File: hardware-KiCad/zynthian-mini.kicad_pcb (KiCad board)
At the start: 2 copper layers, 163 x 120 mm, 76 parts, among them SW1 SW_Push, SW10 SW_Push, SW11 SW_Push, SW12 SW_Push, SW13 SW_Push, SW14 SW_Push, SW15 SW_Push, SW16 SW_Push, SW17 SW_Push, SW18 SW_Push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

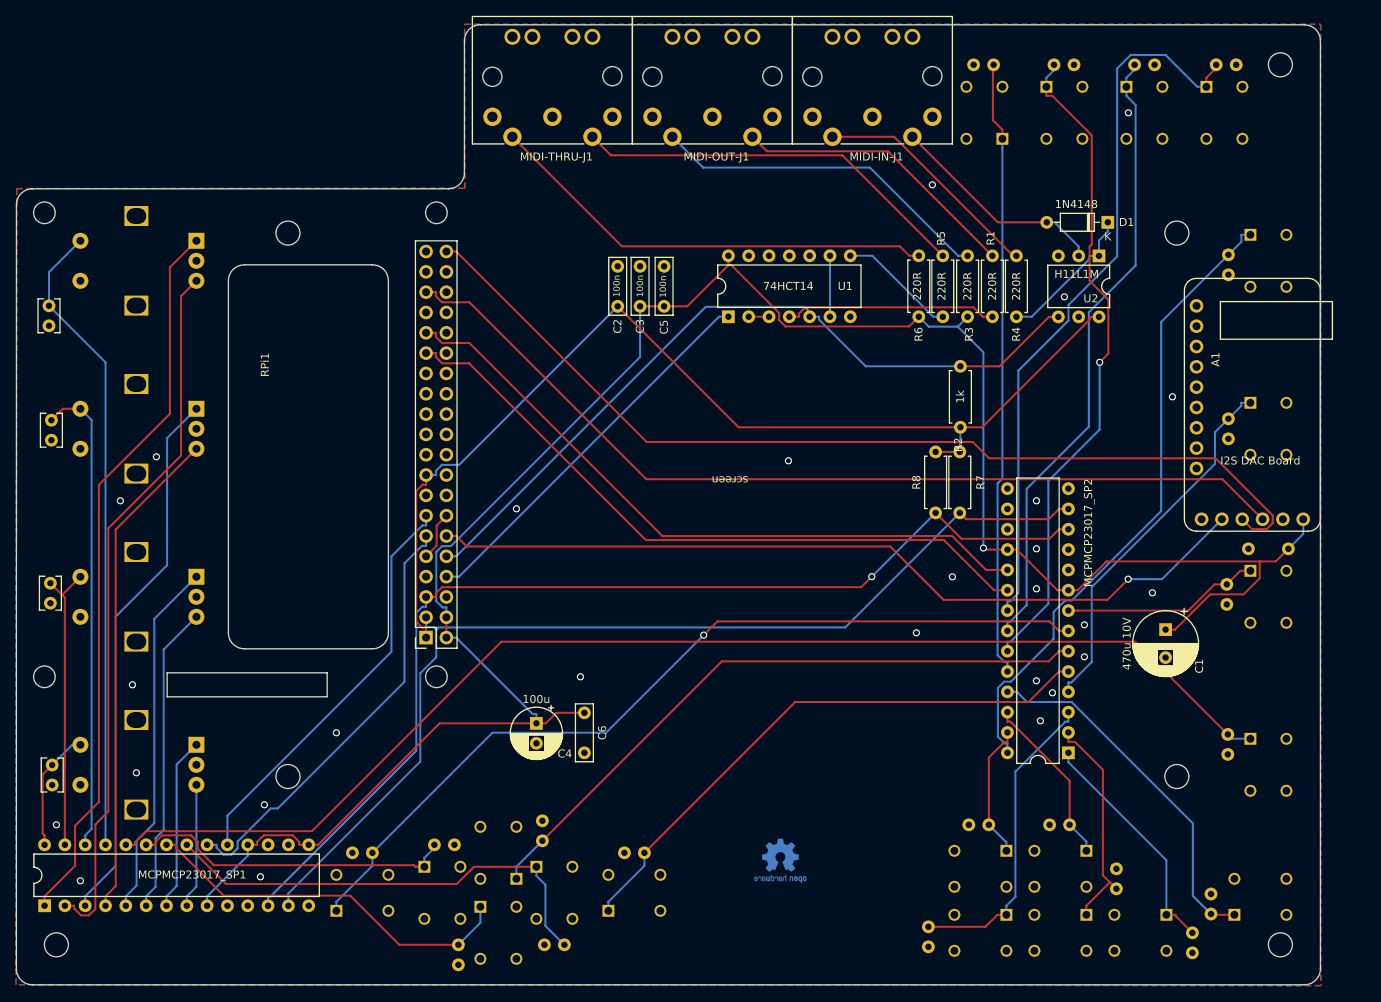
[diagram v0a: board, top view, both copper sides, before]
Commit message: added RCA, Neutrik and HAT connector
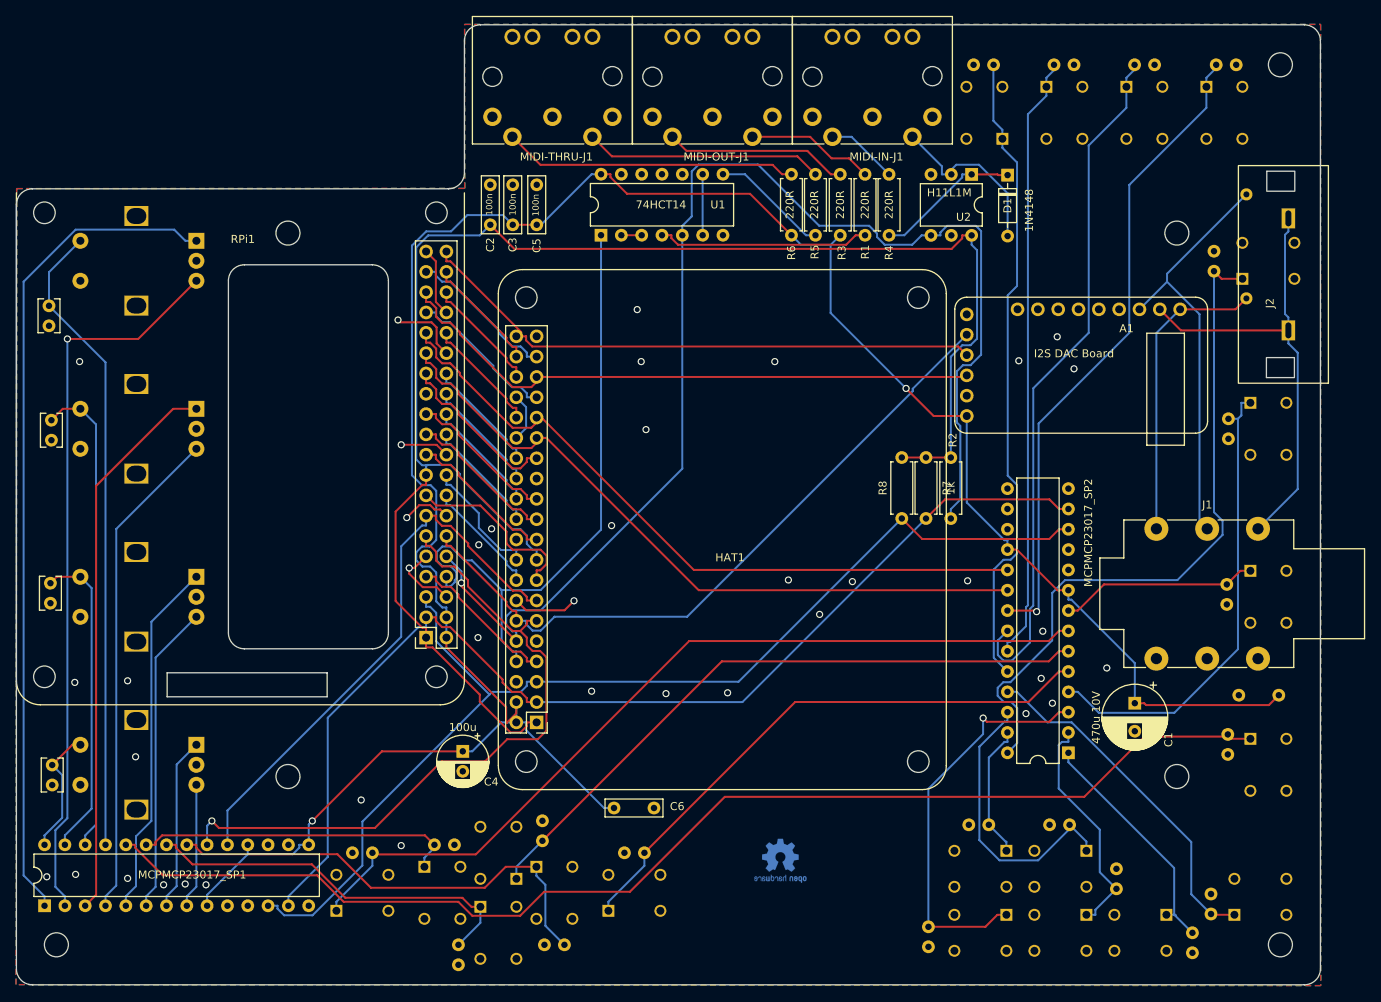
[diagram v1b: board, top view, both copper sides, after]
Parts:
- added HAT1: RPI HAT Connector, project-footprints:raspberry pi 4, F.Cu at (121.7, 108.5)
- added J1: NEUTRIK, Connector_Audio:Jack_6.35mm_Neutrik_NMJ6HFD2_Horizontal, F.Cu at (175.9, 98.4)
- added J2: RCA RS-234, project-footprints:RCA RS-234, F.Cu at (191.4, 66.6)
- moved A1 22.0 mm to (166.5, 77.9), turned to 0 degrees
- moved R5 18.9 mm to (133.3, 54.1)
- moved R6 18.9 mm to (130.3, 61.7)
- moved U2 18.9 mm to (152.8, 54.1)
- moved U1 18.9 mm to (106.5, 61.7)
- moved C2 18.9 mm to (92.7, 60.4)
- moved C3 18.9 mm to (95.5, 60.4)
- moved C5 18.9 mm to (98.5, 55.4)
- moved R1 18.9 mm to (139.5, 54.1)
- moved R4 18.9 mm to (142.5, 54.1)
- moved R3 18.9 mm to (136.4, 61.7)
- moved C7 18.3 mm to (191.2, 119.2)
- moved D1 13.8 mm to (157.3, 54.2), turned to -90 degrees
- moved C6 12.5 mm to (108.1, 133.3), turned to 0 degrees
- moved C1 9.97 mm to (173.2, 120.2)
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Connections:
- A1 pad 7: unconnected-(A1-LOUT-Pad7) -> AUDIO_L_OUT
- A1 pad 8: unconnected-(A1-AGND-Pad8) -> AUDIO_GND_OUT
- A1 pad 9: unconnected-(A1-ROUT-Pad9) -> AUDIO_R_OUT
- RPi1 pad 15: unconnected-(RPi1-Pin_15-Pad15) -> GPIO22(GEN3)
- RPi1 pad 16: unconnected-(RPi1-Pin_16-Pad16) -> GPIO23(GEN4)
- RPi1 pad 18: unconnected-(RPi1-Pin_18-Pad18) -> GPIO24(GEN5)
- RPi1 pad 19: unconnected-(RPi1-Pin_19-Pad19) -> GPIO10(SPI0_MOSI)
- RPi1 pad 21: unconnected-(RPi1-Pin_21-Pad21) -> GPIO9(SPI0_MISO)
- RPi1 pad 22: unconnected-(RPi1-Pin_22-Pad22) -> GPIO25(GEN6)
- RPi1 pad 23: unconnected-(RPi1-Pin_23-Pad23) -> GPIO11(SPI0_SCK)
- RPi1 pad 24: unconnected-(RPi1-Pin_24-Pad24) -> GPIO8(SPI0_CE_N)
- RPi1 pad 26: unconnected-(RPi1-Pin_26-Pad26) -> GPIO7(SPI1_CE_N)
- RPi1 pad 27: unconnected-(RPi1-Pin_27-Pad27) -> ID_SD
- RPi1 pad 28: unconnected-(RPi1-Pin_28-Pad28) -> ID_SC
- RPi1 pad 32: unconnected-(RPi1-Pin_32-Pad32) -> GPIO12(PWM0)
- RPi1 pad 33: unconnected-(RPi1-Pin_33-Pad33) -> GPIO13(PWM1)
- RPi1 pad 36: unconnected-(RPi1-Pin_36-Pad36) -> GPIO16
- RPi1 pad 37: unconnected-(RPi1-Pin_37-Pad37) -> GPIO26
- RPi1 pad 38: unconnected-(RPi1-Pin_38-Pad38) -> GPIO20(SPI1_MOSI)
- RPi1 pad 7: unconnected-(RPi1-Pin_7-Pad7) -> GPIO4(GCLK)
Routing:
- net MIDI_IN: track 95.9 -> 166.2 mm, vias 0 -> 1
- net +3.3V: track 133.4 -> 203.3 mm
- net AUDIO_GND_OUT: track 0.00 -> 58.9 mm
- net AUDIO_R_OUT: track 0.00 -> 52.9 mm
- net I2S_AUDIO_OUT_DATA: track 122.5 -> 72.3 mm
- net GND: track 6.13 -> 53.5 mm, vias 27 -> 38
- net I2S_LRCLK: track 116.6 -> 75.2 mm
- net AUDIO_L_OUT: track 0.00 -> 37.5 mm
- net MIDI_OUT: track 48.7 -> 80.9 mm
- net INT3: track 54.5 -> 86.2 mm, vias 0 -> 1
- net +5V: track 271.8 -> 301.9 mm, vias 1 -> 2
- net GPIO22(GEN3): track 0.00 -> 22.9 mm
- net ID_SD: track 0.00 -> 21.1 mm
- net Net-(MIDI-THRU-J1-Pad4): track 57.0 -> 36.8 mm
- net Net-(MIDI-THRU-J1-Pad5): track 50.0 -> 29.8 mm
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
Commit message: added encoder de bouncing caps
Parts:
- added C28: 10n, Capacitor_THT:C_Rect_L4.0mm_W2.5mm_P2.50mm, F.Cu at (42.9, 149.6)
- added C29: 10n, Capacitor_THT:C_Rect_L4.0mm_W2.5mm_P2.50mm, F.Cu at (46.1, 149.6)
- added C30: 10n, Capacitor_THT:C_Rect_L4.0mm_W2.5mm_P2.50mm, F.Cu at (49.3, 149.7)
- added C35: 10n, Capacitor_THT:C_Rect_L4.0mm_W2.5mm_P2.50mm, F.Cu at (52.5, 149.7)
- added C36: 10n, Capacitor_THT:C_Rect_L4.0mm_W2.5mm_P2.50mm, F.Cu at (55.6, 149.7)
- added C37: 10n, Capacitor_THT:C_Rect_L4.0mm_W2.5mm_P2.50mm, F.Cu at (58.7, 149.7)
- added C38: 10n, Capacitor_THT:C_Rect_L4.0mm_W2.5mm_P2.50mm, F.Cu at (61.8, 149.7)
- added C39: 10n, Capacitor_THT:C_Rect_L4.0mm_W2.5mm_P2.50mm, F.Cu at (64.9, 149.7)
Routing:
- net ENC-B-4: track 15.6 -> 27.5 mm
- net ENC-A-4: track 21.7 -> 33.0 mm
- net ENC-B-3: track 38.7 -> 49.5 mm
- net ENC-A-3: track 44.8 -> 55.0 mm
- net ENC-B-2: track 61.8 -> 71.5 mm
- net ENC-A-2: track 69.6 -> 78.6 mm
- net ENC-B-1: track 91.1 -> 99.5 mm
- net ENC-A-1: track 104.0 -> 111.6 mm
